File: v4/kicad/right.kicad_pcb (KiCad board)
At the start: 2 copper layers, 158.5 x 119.3 mm, 72 parts

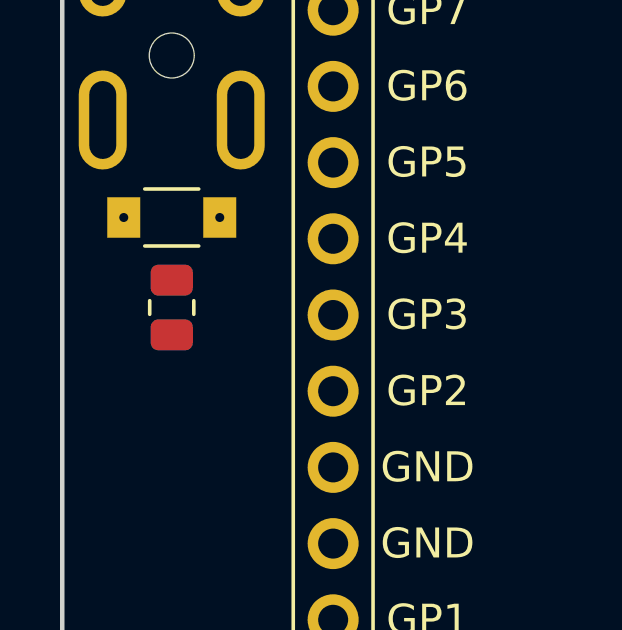
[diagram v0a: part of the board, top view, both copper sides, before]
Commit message: Finalize v4 TRRS protection placement clearance
Move data_resistor down 0.5mm (shift_y 15-17 -> 15-17.5, both halves) so
the TVS<->resistor courtyard gap is 0.67mm (was 0.17mm after the sod-123fl
land-pattern update grew the TVS courtyard). All clearances verified: TVS
0.75mm from the jack, ~28mm of open board below, both parts within the
outline. Regenerate and re-sync v4/kicad.
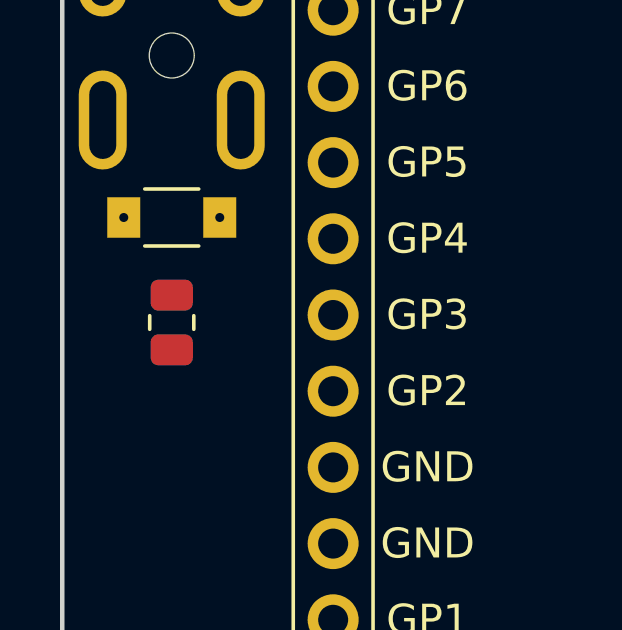
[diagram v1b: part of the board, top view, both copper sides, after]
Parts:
- moved SMD1 0.50 mm to (228.1, 118.0)

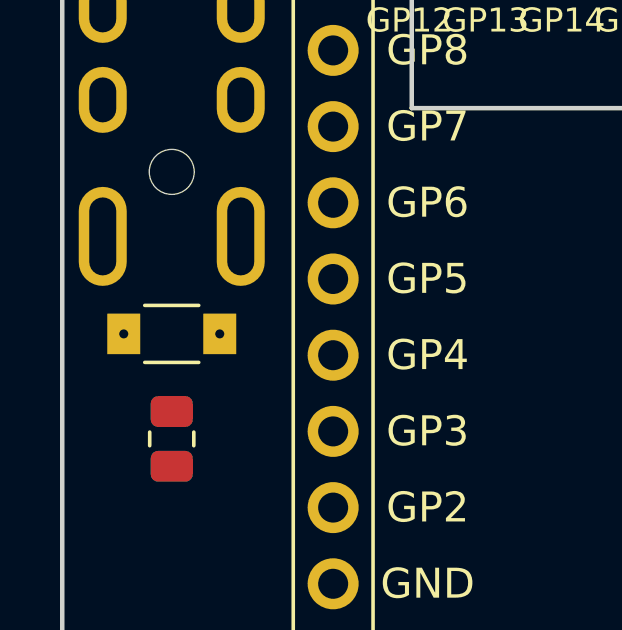
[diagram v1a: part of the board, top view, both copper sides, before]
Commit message: Label v4 TRRS protection parts descriptively
TVS (sod-123fl): name pads K (cathode/'to') and A (anode/'from') instead
of 1/2, set the value to SMF3.3CA, and document the params/pads in comments.
Resistor (smd_0805): override designator to R (R1, not the generic SMD1)
and add a '100R' silk value label. Document each part's pad->net mapping
in the ergogen config comments.
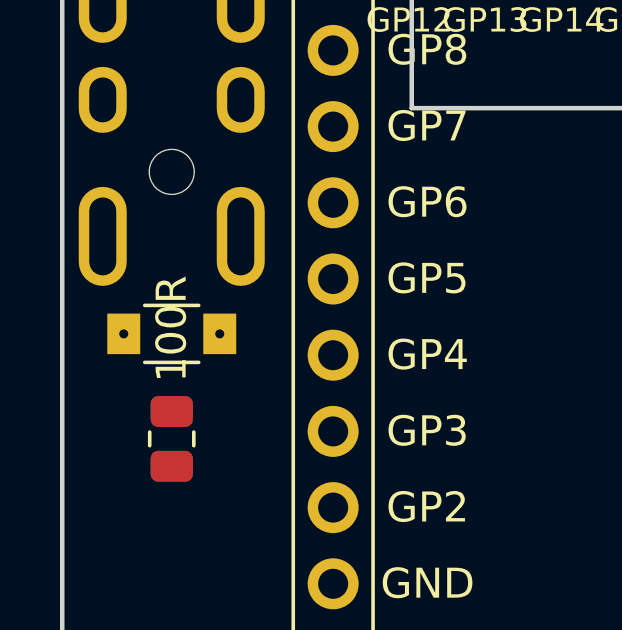
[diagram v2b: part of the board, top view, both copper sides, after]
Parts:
- removed SMD1: , smd_805
- added R1: , smd_805, F.Cu at (228.1, 118.0)
- D33: value SOD-123FL -> SMF3.3CA

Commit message: Sync v4 kicad working PCBs with finalized TRRS protection placement
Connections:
- TRRS1 pad 2: DATA_RAW -> GND
- TRRS1 pad 3: GND -> DATA_RAW

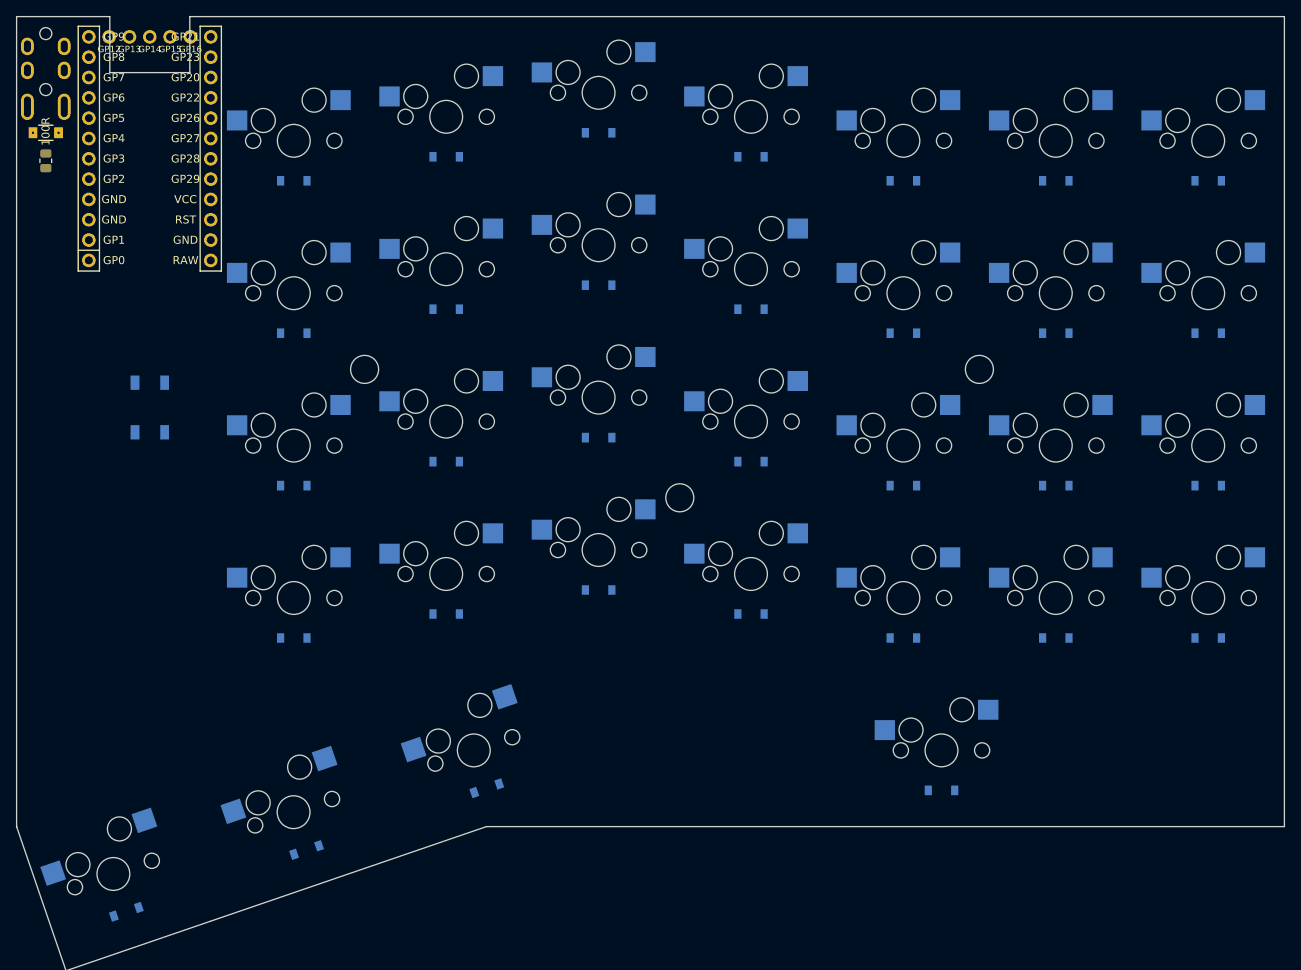
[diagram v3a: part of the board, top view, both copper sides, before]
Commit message: Tune v4 TRRS protection placement and update routed PCBs
Move data_tvs/data_resistor shifts (resistor to a ~2.38mm gap matching the MCU-TVS gap) on both halves, plus YAML formatting cleanup. Refresh left/right kicad PCBs.
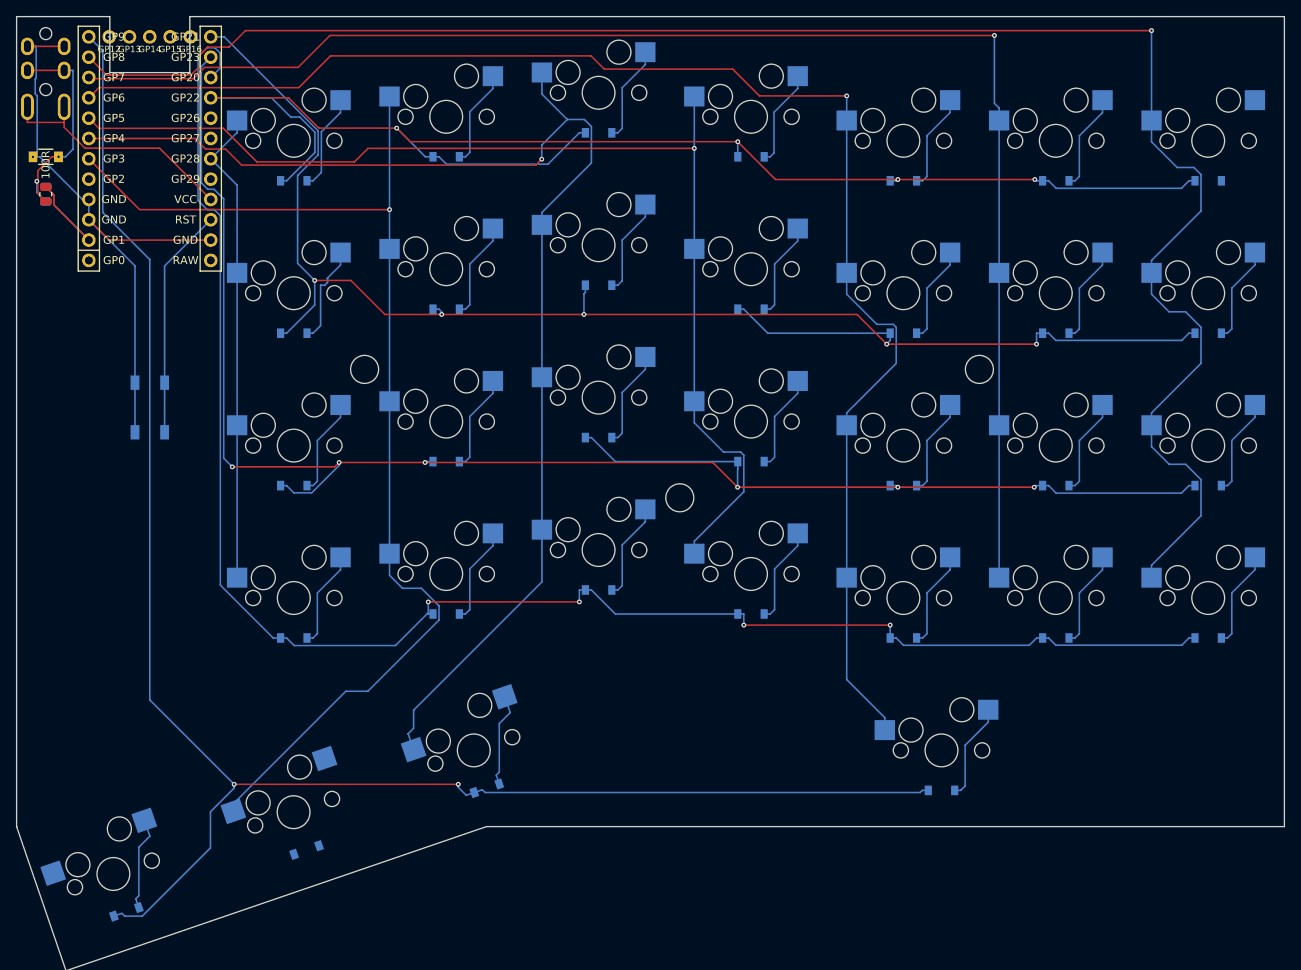
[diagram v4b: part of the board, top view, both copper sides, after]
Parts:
- moved R1 4.17 mm to (228.1, 122.2)
- moved D33 3.00 mm to (228.1, 117.5)
- turned D32 to 19 degrees
- turned D30 to 19 degrees
- turned D31 to 19 degrees
- turned S32 to 19 degrees
- turned S31 to 19 degrees
- turned S30 to 19 degrees
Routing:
- net P8: track 0.00 -> 224.3 mm, vias 0 -> 1
- net P9: track 0.00 -> 213.9 mm, vias 0 -> 2
- net P16: track 0.00 -> 211.5 mm, vias 0 -> 6
- net P14: track 0.00 -> 210.8 mm, vias 0 -> 4
- net P10: track 0.00 -> 190.3 mm, vias 0 -> 5
- net P6: track 0.00 -> 186.5 mm, vias 0 -> 1
- net P7: track 0.00 -> 183.5 mm, vias 0 -> 1
- net P15: track 0.00 -> 181.2 mm, vias 0 -> 4
- net P4: track 0.00 -> 162.6 mm, vias 0 -> 1
- net P3: track 0.00 -> 145.8 mm, vias 0 -> 1
- net P5: track 0.00 -> 142.2 mm, vias 0 -> 1
- net GND: track 0.00 -> 76.6 mm
- net P20: track 0.00 -> 59.9 mm
- net VCC: track 0.00 -> 31.2 mm
- net RST: track 0.00 -> 29.0 mm
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
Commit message: Regenerate v4 PCBs and add routed masters with GND pour
Regenerate left/right working boards from the updated ergogen config and add the
v4/kicad/routed/ masters (the fab source), each carrying the B.Cu GND pour added
by copy-pcbs-kicad-to-routed.
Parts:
- MCU1: moved to B.Cu
- moved MH3 170.8 mm to (174.3, 132.4)
- moved B1 95.0 mm to (147.5, 132.4)
- moved D33 94.4 mm to (134.5, 104.8), turned to 180 degrees
- moved D30 94.3 mm to (189.6, 184.7), turned to 18.925 degrees
- moved D31 94.3 mm to (167.1, 192.5), turned to 18.925 degrees
- moved D32 94.3 mm to (144.6, 200.2), turned to 18.925 degrees
- moved D1 94.3 mm to (222.7, 162.9)
- moved D17 94.3 mm to (246.5, 185.0)
- moved D2 94.3 mm to (222.7, 143.9)
- moved D3 94.3 mm to (222.7, 124.8)
- moved D4 94.3 mm to (222.7, 105.8)
- moved D5 94.3 mm to (203.6, 159.9)
- moved D6 94.3 mm to (203.6, 140.9)
- moved D7 94.3 mm to (203.6, 121.8)
- moved D8 94.3 mm to (203.6, 102.8)
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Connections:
- net dash_bottom renamed dash_lower
- net dash_number renamed dash_num
- net dash_top renamed dash_upper
- net equal_bottom renamed equal_lower
- net equal_number renamed equal_num
- net equal_top renamed equal_upper
- net mirror_five_bottom renamed mirror_five_lower
- net mirror_five_meta renamed mirror_five_mod
- net mirror_five_number renamed mirror_five_num
- net mirror_five_top renamed mirror_five_upper
- net mirror_four_bottom renamed mirror_four_lower
- net mirror_four_meta renamed mirror_four_mod
- net mirror_four_number renamed mirror_four_num
- net mirror_four_top renamed mirror_four_upper
- net mirror_three_bottom renamed mirror_three_lower
- net mirror_three_meta renamed mirror_three_mod
- net mirror_three_number renamed mirror_three_num
- net mirror_three_top renamed mirror_three_upper
- net mirror_two_bottom renamed mirror_two_lower
- net mirror_two_number renamed mirror_two_num
- net mirror_two_top renamed mirror_two_upper
- net zero_bottom renamed zero_lower
- net zero_meta renamed zero_mod
- net zero_number renamed zero_num
- net zero_top renamed zero_upper
- MCU1 pad 1: P1 -> RAW
- MCU1 pad 10: P7 -> P14
- MCU1 pad 11: P8 -> P16
- MCU1 pad 12: P9 -> P10
- MCU1 pad 13: P10 -> P9
- MCU1 pad 14: P16 -> P8
- MCU1 pad 15: P14 -> P7
- MCU1 pad 16: P15 -> P6
- MCU1 pad 17: P18 -> P5
- MCU1 pad 18: P19 -> P4
- MCU1 pad 19: P20 -> P3
- MCU1 pad 2: P0 -> GND
- MCU1 pad 20: P21 -> P2
- MCU1 pad 21: VCC -> GND
- MCU1 pad 22: RST -> GND
- MCU1 pad 23: GND -> P0
- MCU1 pad 24: RAW -> P1
- MCU1 pad 3: GND -> RST
- MCU1 pad 4: GND -> VCC
- MCU1 pad 5: P2 -> P21
- MCU1 pad 6: P3 -> P20
- MCU1 pad 7: P4 -> P19
- MCU1 pad 8: P5 -> P18
- MCU1 pad 9: P6 -> P15
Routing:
- net P8: track 224.3 -> 0.00 mm, vias 1 -> 0
- net P9: track 213.9 -> 0.00 mm, vias 2 -> 0
- net P16: track 211.5 -> 0.00 mm, vias 6 -> 0
- net P14: track 210.8 -> 0.00 mm, vias 4 -> 0
- net P10: track 190.3 -> 0.00 mm, vias 5 -> 0
- net P6: track 186.5 -> 0.00 mm, vias 1 -> 0
- net P7: track 183.5 -> 0.00 mm, vias 1 -> 0
- net P15: track 181.2 -> 0.00 mm, vias 4 -> 0
- net P4: track 162.6 -> 0.00 mm, vias 1 -> 0
- net P3: track 145.8 -> 0.00 mm, vias 1 -> 0
- net P5: track 142.2 -> 0.00 mm, vias 1 -> 0
- net GND: track 76.6 -> 0.00 mm
- net P20: track 59.9 -> 0.00 mm
- net VCC: track 31.2 -> 0.00 mm
- net RST: track 29.0 -> 0.00 mm
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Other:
- board size 158.5 x 119.3 mm -> 158 x 119 mm
- board text added: ""Splinter" keyboard v4 by @andornaut"
- board text added: "100R Panasonic ERJ-6ENF 1000V"
- board text added: "M3x0.5"
- board text added: "Reset switch E-Switch TL3342F450QG"
- board text added: "TRRS"
- board text added: "TVS Littelfuse SMF3.3CA"
- board text added: "https://github.com/andornaut/splinter-keyboard"
- board text added: "splitkb Liatris"

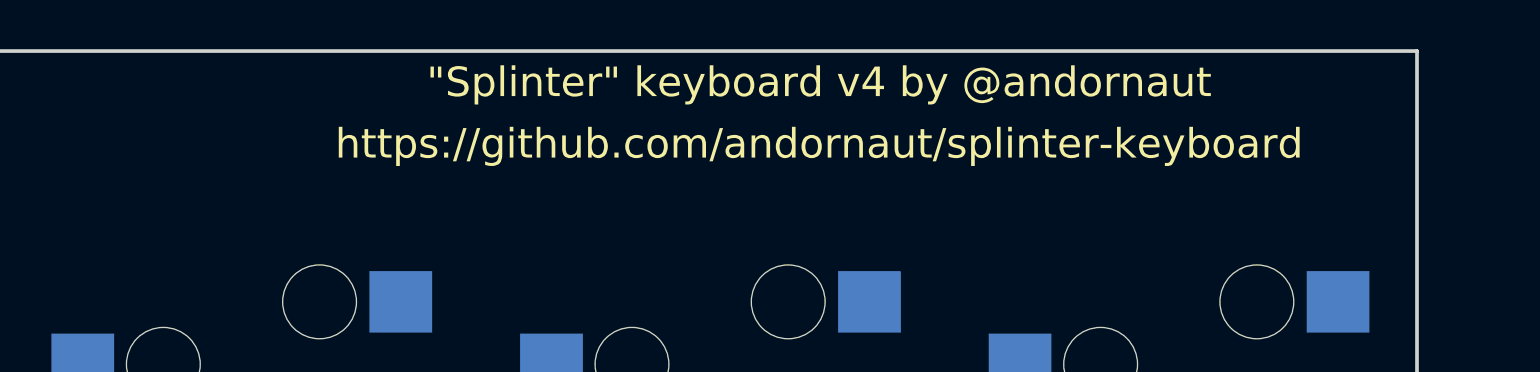
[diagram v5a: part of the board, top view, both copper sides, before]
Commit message: Switch fab pipeline to kicad-cli; add JLCPCB assembly (BOM/CPL)
- fab-jlcpcb.sh now exports gerbers/drill via kicad-cli (drop KiKit) and
  emits per-board BOM/CPL when v4/kicad/jlcpcb-parts.json exists
- Add gen-jlcpcb-bom-cpl.py and jlcpcb-parts.json (LCSC part assignment)
- Refactor v4 ergogen config: per-column/per-row mirror nets, single
  two-line credit text, shared placement x vars
- Regenerate v4 PCBs; update README for KiCad 10 / kicad-cli workflow
- Ignore KiCad .history/ local-history dir
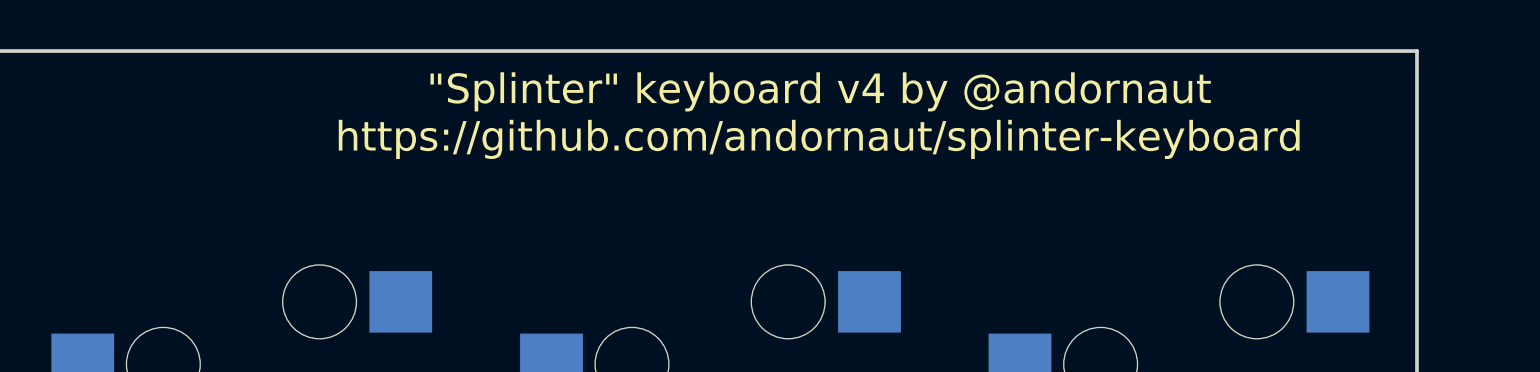
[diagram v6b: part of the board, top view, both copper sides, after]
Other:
- board text added: ""Splinter" keyboard v4 by @andornaut https://github.com/andornaut/splinter-keyboard"
- board text removed: ""Splinter" keyboard v4 by @andornaut"
- board text removed: "https://github.com/andornaut/splinter-keyboard"

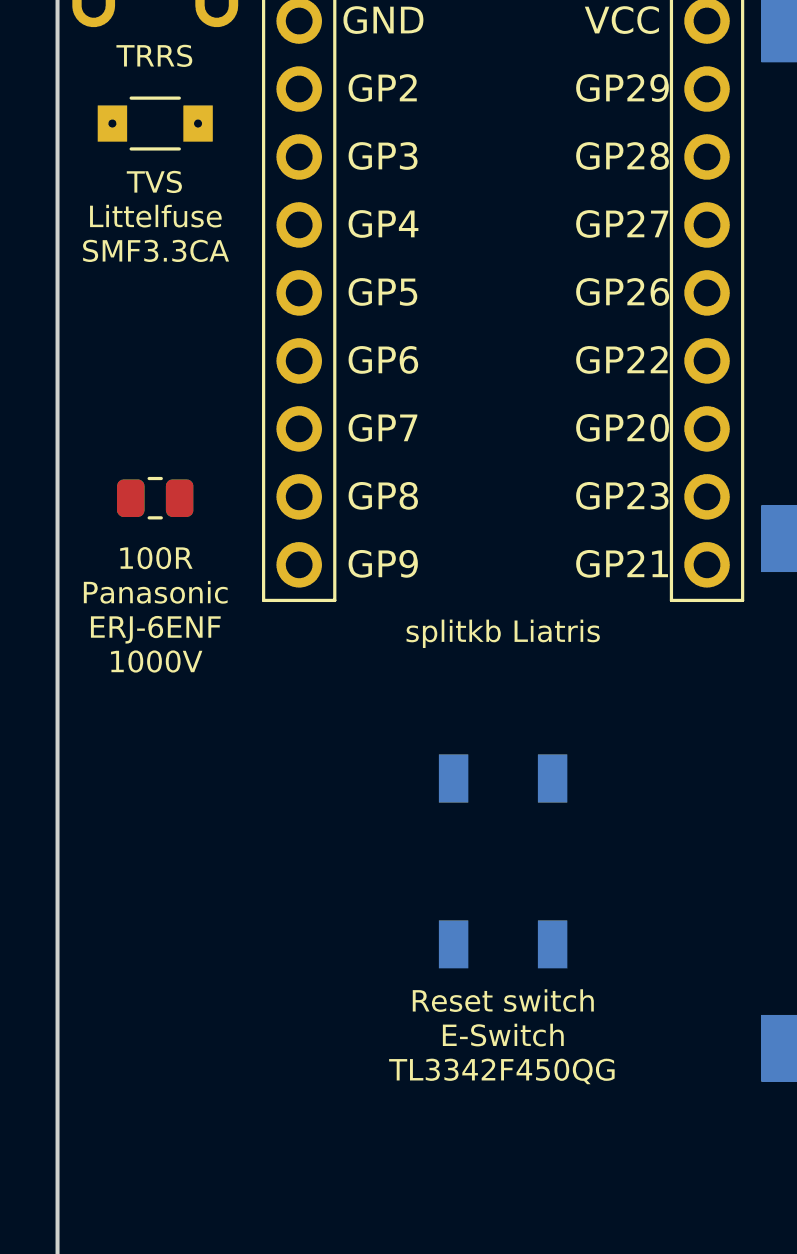
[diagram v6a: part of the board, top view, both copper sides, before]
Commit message: v4: switch data-line TVS to SMF5.0CA; refresh part labels and BOM
Change the data-line TVS from SMF3.3CA to SMF5.0CA (5V standoff) and
update its footprint, silk label, and jlcpcb-parts entry (C1851363).
Refresh reset/diode/resistor silk labels and BOM notes to match the
sourced parts, regenerate the v4 PCBs, and remove README references to
the uncommitted AGENTS.md.
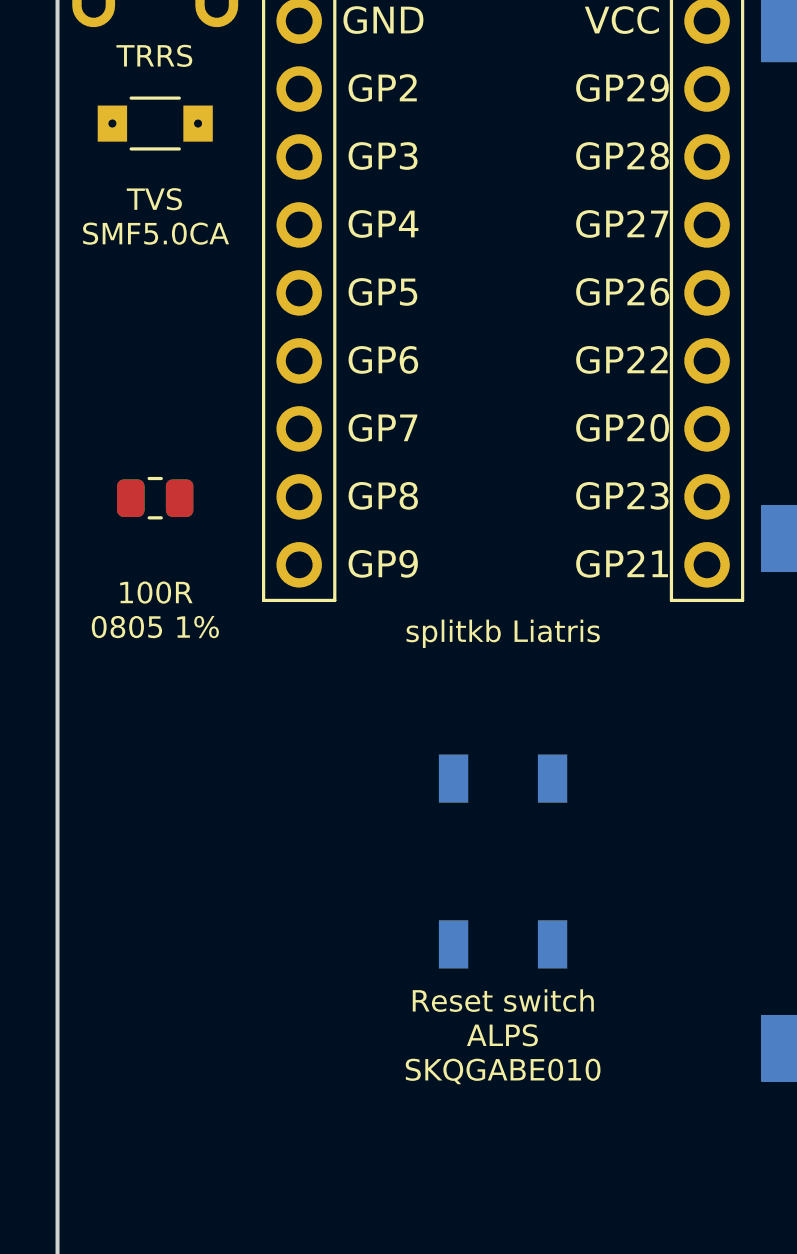
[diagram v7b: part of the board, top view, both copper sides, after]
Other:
- board text added: "100R 0805 1%"
- board text added: "Reset switch ALPS SKQGABE010"
- board text added: "TVS SMF5.0CA"
- board text removed: "100R Panasonic ERJ-6ENF 1000V"
- board text removed: "Reset switch E-Switch TL3342F450QG"
- board text removed: "TVS Littelfuse SMF3.3CA"
